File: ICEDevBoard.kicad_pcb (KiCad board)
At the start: 2 copper layers, 9.2 x 1.8 mm, 233 parts, among them J101 USB4215-03-A_REVA, J301 program, J401 VGA, J501 Joystick, J502 SJ2-35813B-SMT-TR, J503 Keyboard, J504 Mouse, J505 MSD-1-A, J701 PMOD, Q101 BC847, SW701 SW_Push, SW702 SW_Push, SW703 SW_Push, U101 AP2127K-3.3, U102 AP2127K-2.5, U103 AP2127K-1.2, U201 93LC56BT-I/OT, U202 FT232H, U301 ICE40HX8K-BG121, U302 W25Q32JVSS, U401 ADV7123, U501 SN74LVC8T245PWR, U502 PCM5102A, U503 SN74LV1T34DBV, U601 IS61WV5128EDBLL-10TLI, U701 74AHC595, U702 74AHC595, Y201 12Mhz, Y301 50Mhz, Y302 12Mhz

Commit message: Started layout
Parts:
- moved H104 414.1 mm to (192.0, 142.0)
- moved H102 391.0 mm to (192.0, 58.0)
- moved C105 345.8 mm to (116.5, 127.5), turned to -90 degrees
- moved H103 344.7 mm to (107.0, 142.0)
- moved C107 339.4 mm to (116.5, 123.5), turned to -90 degrees
- moved D104 338.0 mm to (112.5, 125.5), turned to 180 degrees
- moved R103 336.5 mm to (112.6, 130.5)
- moved L101 335.6 mm to (111.4, 118.0)
- moved R105 330.7 mm to (112.4, 122.0)
- moved TP103 329.2 mm to (115.5, 118.0)
- moved C109 327.0 mm to (106.5, 118.0)
- moved J101 318.3 mm to (102.5, 125.7), turned to -90 degrees
- moved H101 314.5 mm to (107.0, 58.0)
- moved C201 249.7 mm to (115.5, 157.3)
- moved C205 249.7 mm to (115.5, 166.3)
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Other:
- board size 9.2 x 1.8 mm -> 100 x 100 mm

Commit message: Working on board layout
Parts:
- D101, D102, D103, D201, D202, D301, D703, D704, D705: footprint LED_SMD:LED_1210_3225Metric -> LED_SMD:LED_1206_3216Metric
- J401: footprint Connector_Dsub:DSUB-15-HD_Pins_Horizontal_P2.29x2.54mm_EdgePinOffset8.35mm_Housed_MountingHolesOffset10.89mm -> Connector_Dsub:DSUB-15-HD_Socket_Horizontal_P2.29x2.54mm_EdgePinOffset8.35mm_Housed_MountingHolesOffset10.89mm
- moved C512 360.7 mm to (197.4, 136.2)
- moved C513 357.8 mm to (197.4, 123.6), turned to 180 degrees
- moved R101 354.7 mm to (102.5, 110.2)
- moved R102 352.5 mm to (102.4, 106.2)
- moved C509 351.1 mm to (183.1, 134.4)
- moved D105 350.8 mm to (107.0, 98.4)
- moved D101 350.6 mm to (107.0, 110.2)
- moved R104 349.7 mm to (102.4, 102.2)
- moved C508 349.1 mm to (179.3, 134.4)
- moved J502 346.3 mm to (191.4, 129.7), turned to 180 degrees
- moved C507 346.3 mm to (174.1, 135.1)
- moved R107 345.1 mm to (102.5, 98.4)
- moved R106 345.0 mm to (102.7, 94.3)
- moved D102 345.0 mm to (107.0, 106.2)
- moved Q101 344.1 mm to (107.0, 94.0)
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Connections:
- R101 pad 1: Net-(D101-K) -> GND
- R101 pad 2: GND -> Net-(D101-K)

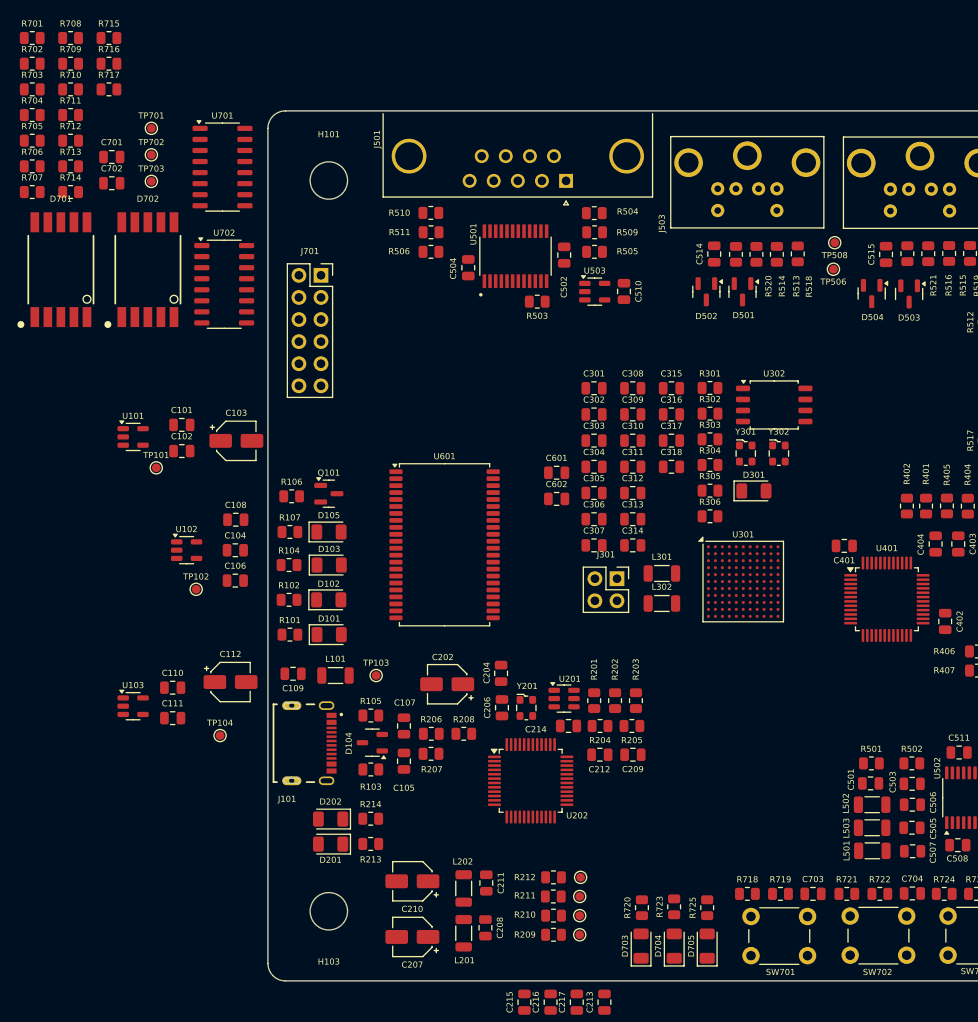
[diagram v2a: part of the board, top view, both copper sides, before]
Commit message: More board layout
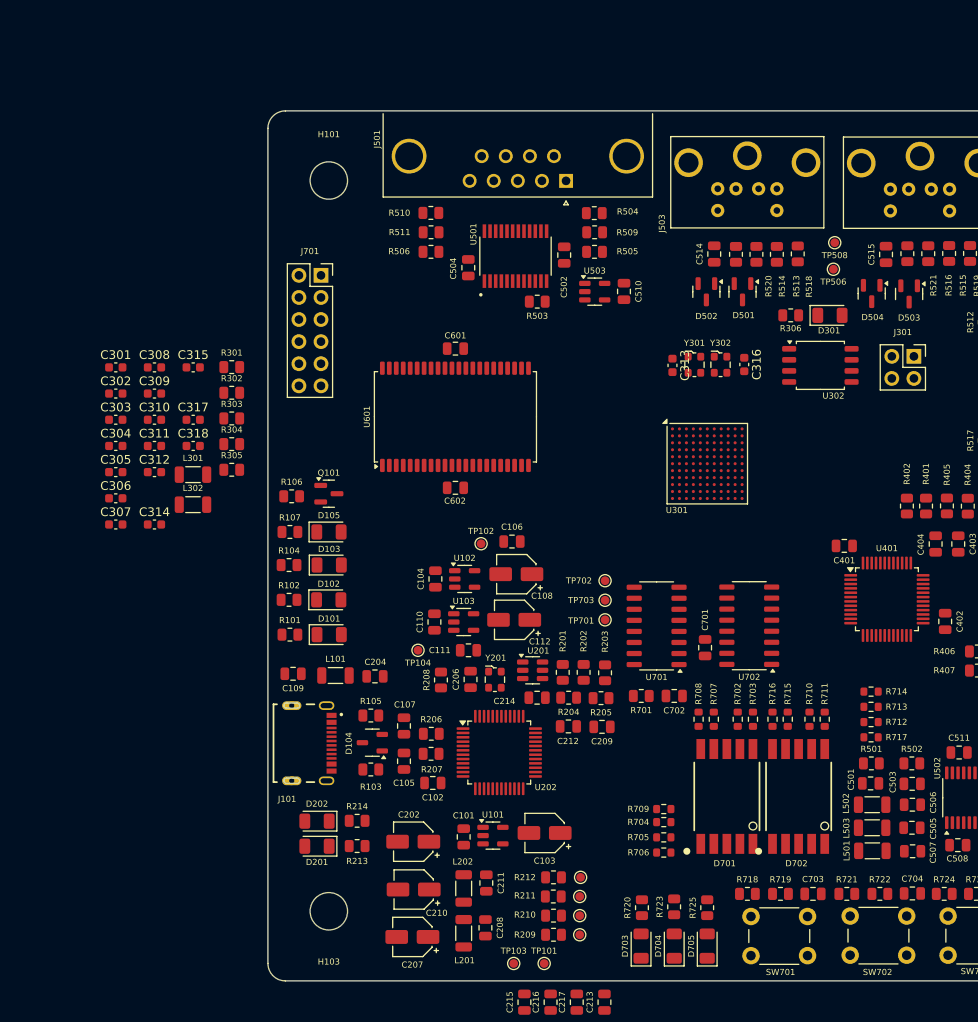
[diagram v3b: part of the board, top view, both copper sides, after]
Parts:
- C108: footprint Capacitor_SMD:C_0805_2012Metric -> Capacitor_SMD:CP_Elec_4x5.3
- C301, C302, C303, C304, C305, C306, C307, C308, C309, C310, C311, C312, C313, C314, C315, C316, C317, C318: footprint Capacitor_SMD:C_0805_2012Metric -> Capacitor_SMD:C_0603_1608Metric
- R206, R207: value 0R -> 22R
- R702, R703, R704, R705, R706, R707, R708, R709, R710, R711, R712, R713, R714, R715, R716, R717: footprint Resistor_SMD:R_0805_2012Metric -> Resistor_SMD:R_0603_1608Metric
- moved R717 115.0 mm to (169.3, 122.0)
- moved R712 113.7 mm to (169.3, 120.2), turned to 180 degrees
- moved R710 111.6 mm to (162.2, 119.9), turned to -90 degrees
- moved R711 111.1 mm to (164.0, 119.9), turned to -90 degrees
- moved R713 111.0 mm to (169.3, 118.5), turned to 180 degrees
- moved R702 110.7 mm to (154.0, 119.9), turned to -90 degrees
- moved R715 110.5 mm to (159.8, 119.9), turned to 90 degrees
- moved R703 110.0 mm to (155.8, 119.9), turned to -90 degrees
- moved R709 109.5 mm to (145.5, 130.2)
- moved R704 109.0 mm to (145.5, 131.8)
- moved R714 108.5 mm to (169.3, 116.8), turned to 180 degrees
- moved R705 108.1 mm to (145.5, 133.5)
- moved R716 107.2 mm to (158.0, 119.9), turned to -90 degrees
- moved R706 107.2 mm to (145.5, 135.2)
- moved R708 106.5 mm to (149.5, 119.9), turned to -90 degrees
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
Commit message: Started FPGA fanout
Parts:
- R702, R703, R704, R705, R706, R707, R708, R709, R710, R711, R712, R713, R714, R715, R716, R717: footprint Resistor_SMD:R_0603_1608Metric -> Resistor_SMD:R_0805_2012Metric
- moved C302 11.2 mm to (83.5, 93.7)
- moved C309 11.2 mm to (88.0, 93.7)
- moved R303 11.2 mm to (96.9, 96.5)
- moved C301 11.2 mm to (83.5, 90.7)
- moved C303 11.2 mm to (83.5, 96.7)
- moved C304 11.2 mm to (83.5, 99.7)
- moved C305 11.2 mm to (83.5, 102.7)
- moved C306 11.2 mm to (83.5, 105.7)
- moved C307 11.2 mm to (83.5, 108.7)
- moved C308 11.2 mm to (88.0, 90.7)
- moved C310 11.2 mm to (88.0, 96.7)
- moved C311 11.2 mm to (88.0, 99.7)
- moved C312 11.2 mm to (88.0, 102.7)
- moved C314 11.2 mm to (88.0, 108.7)
- moved C315 11.2 mm to (92.5, 90.7)
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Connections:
- U301 pad A1: /FPGA/PMOD3 -> unconnected-(U301A-IOT_225-PadA1)
- U301 pad A10: /FPGA/MEM_A1 -> unconnected-(U301A-IOT_170-PadA10)
- U301 pad A11: /FPGA/MEM_A0 -> unconnected-(U301A-IOT_168-PadA11)
- U301 pad A2: /FPGA/PMOD1 -> unconnected-(U301A-IOT_222-PadA2)
- U301 pad A3: /FPGA/PMOD2 -> unconnected-(U301A-IOT_223-PadA3)
- U301 pad A4: /FPGA/MEM_A16 -> unconnected-(U301A-IOT_211-PadA4)
- U301 pad A5: /FPGA/MEM_A14 -> unconnected-(U301A-IOT_207-PadA5)
- U301 pad A6: /FPGA/MEM_A13 -> unconnected-(U301A-IOT_206-PadA6)
- U301 pad A7: /FPGA/MEM_A10 -> unconnected-(U301A-IOT_192-PadA7)
- U301 pad A8: /FPGA/MEM_A8 -> unconnected-(U301A-IOT_190-PadA8)
- U301 pad A9: /FPGA/MEM_A5 -> unconnected-(U301A-IOT_178-PadA9)
- U301 pad B1: /FPGA/VGA_R0 -> unconnected-(U301D-IOL_2A-PadB1)
- U301 pad B11: /FPGA/PMOD4 -> unconnected-(U301B-IOR_161-PadB11)
- U301 pad B2: /FPGA/VGA_R1 -> unconnected-(U301D-IOL_2B-PadB2)
- U301 pad B3: /FPGA/PMOD0 -> unconnected-(U301A-IOT_221-PadB3)
- U301 pad B4: /FPGA/MEM_A18 -> unconnected-(U301A-IOT_219-PadB4)
- U301 pad B5: /FPGA/MEM_A15 -> unconnected-(U301A-IOT_208-PadB5)
- U301 pad B8: /FPGA/MEM_A4 -> unconnected-(U301A-IOT_177-PadB8)
- U301 pad B9: /FPGA/MEM_A3 -> unconnected-(U301A-IOT_174-PadB9)
- U301 pad C1: /FPGA/VGA_G0 -> unconnected-(U301D-IOL_5B-PadC1)
- U301 pad C11: /FPGA/JOY_D5 -> unconnected-(U301B-IOR_160-PadC11)
- U301 pad C2: /FPGA/VGA_R4 -> unconnected-(U301D-IOL_5A-PadC2)
- U301 pad C3: /FPGA/VGA_R3 -> unconnected-(U301D-IOL_4B-PadC3)
- U301 pad C4: /FPGA/VGA_R2 -> unconnected-(U301D-IOL_4A-PadC4)
- U301 pad C7: /FPGA/MEM_A9 -> unconnected-(U301A-IOT_191-PadC7)
- U301 pad C8: /FPGA/MEM_A6 -> unconnected-(U301A-IOT_179-PadC8)
- U301 pad C9: /FPGA/MEM_A2 -> unconnected-(U301A-IOT_172-PadC9)
- U301 pad D1: /FPGA/VGA_G2 -> unconnected-(U301D-IOL_8B-PadD1)
- U301 pad D10: /FPGA/JOY_D4 -> unconnected-(U301B-IOR_154-PadD10)
- U301 pad D11: /FPGA/JOY_D3 -> unconnected-(U301B-IOR_152-PadD11)
- U301 pad D2: /FPGA/VGA_G3 -> unconnected-(U301D-IOL_9A-PadD2)
- U301 pad D3: /FPGA/VGA_G4 -> unconnected-(U301D-IOL_9B-PadD3)
- U301 pad D5: /FPGA/MEM_A17 -> unconnected-(U301A-IOT_212-PadD5)
- U301 pad D7: /FPGA/MEM_A7 -> unconnected-(U301A-IOT_181-PadD7)
- U301 pad D9: /FPGA/JOY_D1 -> unconnected-(U301B-IOR_147-PadD9)
- U301 pad E1: /FPGA/VGA_G1 -> unconnected-(U301D-IOL_8A-PadE1)
- U301 pad E10: /FPGA/SND_BCK -> unconnected-(U301B-IOR_141_GBIN2-PadE10)
- U301 pad E11: /FPGA/JOY_D2 -> unconnected-(U301B-IOR_148-PadE11)
- U301 pad E2: /FPGA/VGA_G5 -> unconnected-(U301D-IOL_10A-PadE2)
- U301 pad E3: /FPGA/VGA_B0 -> unconnected-(U301D-IOL_10B-PadE3)
- U301 pad E8: /FPGA/JOY_D0 -> unconnected-(U301B-IOR_146-PadE8)
- U301 pad E9: /FPGA/JOY_SEL -> unconnected-(U301B-IOR_144-PadE9)
- U301 pad F1: /FPGA/VGA_B1 -> unconnected-(U301D-IOL_12A-PadF1)
- U301 pad F10: /FPGA/~{SRAM_WE} -> unconnected-(U301B-IOR_136-PadF10)
- U301 pad F11: /FPGA/SND_DIN -> unconnected-(U301B-IOR_140_GBIN3-PadF11)
- U301 pad F2: /FPGA/VGA_B2 -> unconnected-(U301D-IOL_12B-PadF2)
- U301 pad F3: /FPGA/VGA_B4 -> unconnected-(U301D-IOL_13B_GBIN7-PadF3)
- U301 pad F4: /FPGA/VGA_B3 -> unconnected-(U301D-IOL_13A-PadF4)
- U301 pad F9: /FPGA/SND_LRCK -> unconnected-(U301B-IOR_137-PadF9)
- U301 pad G1: /FPGA/~{VGA_BLANK} -> unconnected-(U301D-IOL_14A_GBIN6-PadG1)
- U301 pad G10: /FPGA/MEM_D6 -> unconnected-(U301B-IOR_120-PadG10)
- U301 pad G11: /FPGA/~{SRAM_CE} -> unconnected-(U301B-IOR_129-PadG11)
- U301 pad G2: /FPGA/VGA_CLOCK -> unconnected-(U301D-IOL_14B-PadG2)
- U301 pad G3: /FPGA/VGA_HSYNC -> unconnected-(U301D-IOL_17A-PadG3)
- U301 pad G8: /FPGA/MEM_D4 -> unconnected-(U301B-IOR_118-PadG8)
- U301 pad G9: /FPGA/MEM_D7 -> unconnected-(U301B-IOR_128-PadG9)
- U301 pad H1: /FPGA/BUTTON1 -> unconnected-(U301D-IOL_18A-PadH1)
- U301 pad H10: /FPGA/MEM_D2 -> unconnected-(U301B-IOR_116-PadH10)
- U301 pad H11: /FPGA/MEM_D5 -> unconnected-(U301B-IOR_119-PadH11)
- U301 pad H2: /FPGA/BUTTON2 -> unconnected-(U301D-IOL_18B-PadH2)
- U301 pad H3: /FPGA/VGA_VSYNC -> unconnected-(U301D-IOL_17B-PadH3)
- U301 pad H7: /FPGA/LED2 -> unconnected-(U301C-IOB_87-PadH7)
- U301 pad H9: /FPGA/PMOD7 -> unconnected-(U301C-IOB_104_CBSEL1-PadH9)
- U301 pad J1: /FPGA/BUTTON3 -> unconnected-(U301D-IOL_23A-PadJ1)
- U301 pad J10: /FPGA/MEM_D3 -> unconnected-(U301B-IOR_117-PadJ10)
- U301 pad J11: /FPGA/MEM_D0 -> unconnected-(U301B-IOR_114-PadJ11)
- U301 pad J2: /FPGA/MEM_A12 -> unconnected-(U301D-IOL_25B-PadJ2)
- U301 pad J3: /FPGA/KBD_DATA -> unconnected-(U301C-IOB_57-PadJ3)
- U301 pad J4: /FPGA/SEG_DATA -> unconnected-(U301C-IOB_64-PadJ4)
- U301 pad J5: /FPGA/SD_MOSI -> unconnected-(U301C-IOB_78-PadJ5)
- U301 pad J7: /FPGA/LED1 -> unconnected-(U301C-IOB_86-PadJ7)
- U301 pad K11: /FPGA/MEM_D1 -> unconnected-(U301B-IOR_115-PadK11)
- U301 pad K2: /FPGA/MEM_A11 -> unconnected-(U301D-IOL_25A-PadK2)
- U301 pad K3: /FPGA/MOUSE_DATA -> unconnected-(U301C-IOB_63-PadK3)
- U301 pad K4: /FPGA/SD_SELECT -> unconnected-(U301C-IOB_73-PadK4)
- U301 pad K5: /FPGA/SD_CLOCK -> unconnected-(U301C-IOB_79-PadK5)
- U301 pad K6: /FPGA/SD_DETECT -> unconnected-(U301C-IOB_82_GBIN4-PadK6)
- U301 pad K7: /FPGA/LED3 -> unconnected-(U301C-IOB_89-PadK7)
- U301 pad L1: /FPGA/KBD_CLK -> unconnected-(U301C-IOB_56-PadL1)
- U301 pad L2: /FPGA/MOUSE_CLK -> unconnected-(U301C-IOB_61-PadL2)
- U301 pad L3: /FPGA/SEG_CLK -> unconnected-(U301C-IOB_71-PadL3)
- U301 pad L4: /FPGA/SEG_LOAD -> unconnected-(U301C-IOB_72-PadL4)
- U301 pad L5: /FPGA/SD_MISO -> unconnected-(U301C-IOB_81_GBIN5-PadL5)
- U301 pad L7: /FPGA/PMOD5 -> unconnected-(U301C-IOB_94-PadL7)
- U301 pad L8: /FPGA/PMOD6 -> unconnected-(U301C-IOB_103_CBSEL0-PadL8)
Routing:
- net unconnected-(U301C-IOB_81_GBIN5-PadL5): track 0.00 -> 1.60 mm
- net unconnected-(U301C-IOB_72-PadL4): track 0.00 -> 1.60 mm
- net unconnected-(U301C-IOB_71-PadL3): track 0.00 -> 1.60 mm
- net unconnected-(U301D-IOL_8B-PadD1): track 0.00 -> 1.55 mm
- net unconnected-(U301D-IOL_8A-PadE1): track 0.00 -> 1.55 mm
- net unconnected-(U301D-IOL_5B-PadC1): track 0.00 -> 1.55 mm
- net unconnected-(U301D-IOL_2A-PadB1): track 0.00 -> 1.55 mm
- net unconnected-(U301D-IOL_23B-PadK1): track 0.00 -> 1.55 mm
- net unconnected-(U301D-IOL_23A-PadJ1): track 0.00 -> 1.55 mm
- net unconnected-(U301D-IOL_18A-PadH1): track 0.00 -> 1.55 mm
- net unconnected-(U301D-IOL_14A_GBIN6-PadG1): track 0.00 -> 1.55 mm
- net unconnected-(U301D-IOL_12A-PadF1): track 0.00 -> 1.55 mm
- net unconnected-(U301B-IOR_161-PadB11): track 0.00 -> 1.55 mm
- net unconnected-(U301B-IOR_160-PadC11): track 0.00 -> 1.55 mm
- net unconnected-(U301B-IOR_148-PadE11): track 0.00 -> 1.55 mm
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- added copper zone on In1.Cu, net GND
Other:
- copper layers 2 -> 4

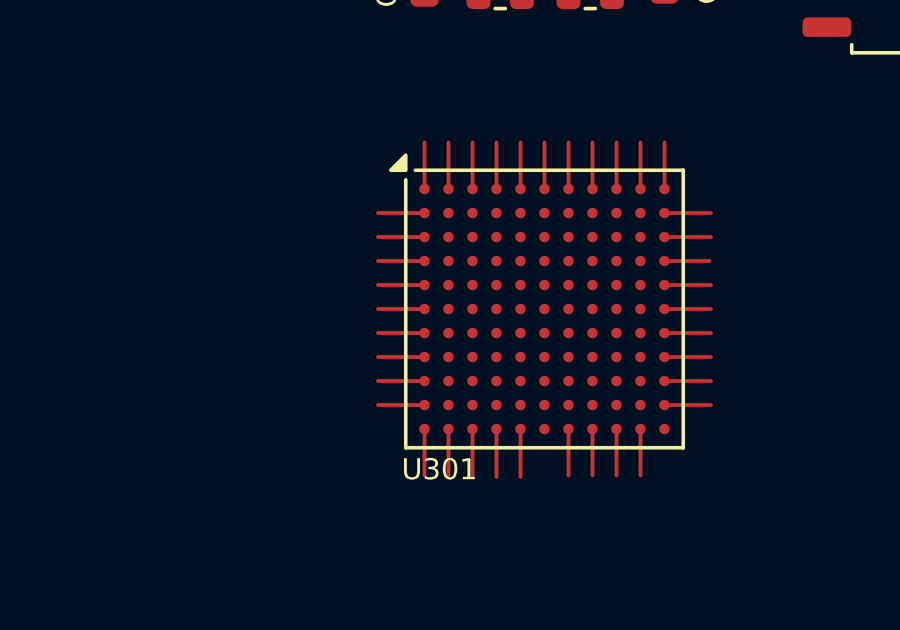
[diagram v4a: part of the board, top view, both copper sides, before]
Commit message: Updated constraints
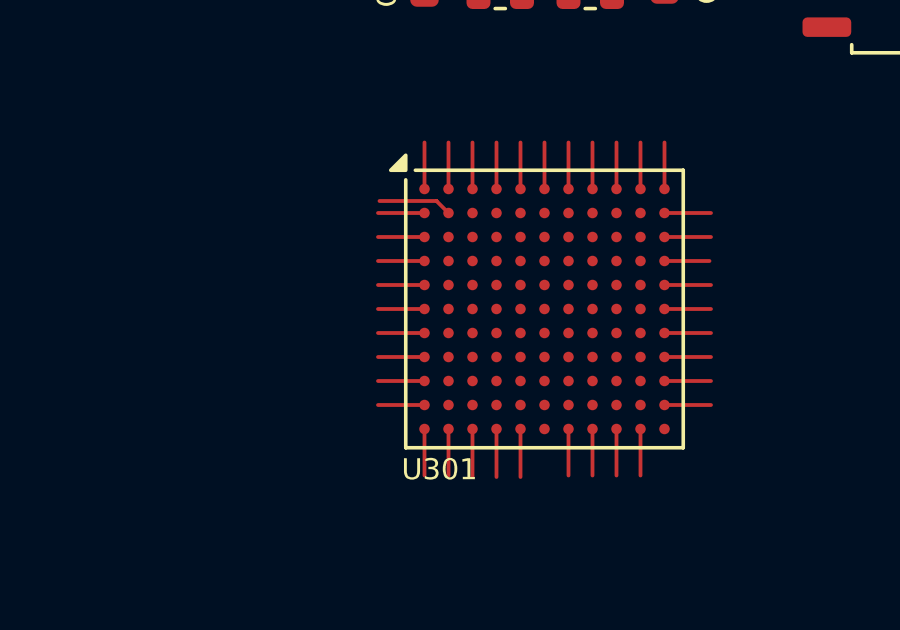
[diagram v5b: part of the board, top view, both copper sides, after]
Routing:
- net unconnected-(U301D-IOL_2B-PadB2): track 0.00 -> 2.47 mm
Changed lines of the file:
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@@
+	)
+	(segment
+		(start 147.3 87.35)
+		(end 146.9 86.95)
+		(width 0.127)
+		(layer "F.Cu")
+		(net 282)
+	)
+	(segment
+		(start 146.9 86.95)
+		(end 145 86.95)
+		(width 0.127)
+		(layer "F.Cu")
+		(net 282)
 	)
 	(segment
@@
 		(width 0.127)
 		(layer "F.Cu")
+		(net 287)
+	)
+	(segment
+		(start 149.7 94.55)
+		(end 149.7 94.527822)
+		(width 0.127)
+		(layer "F.Cu")

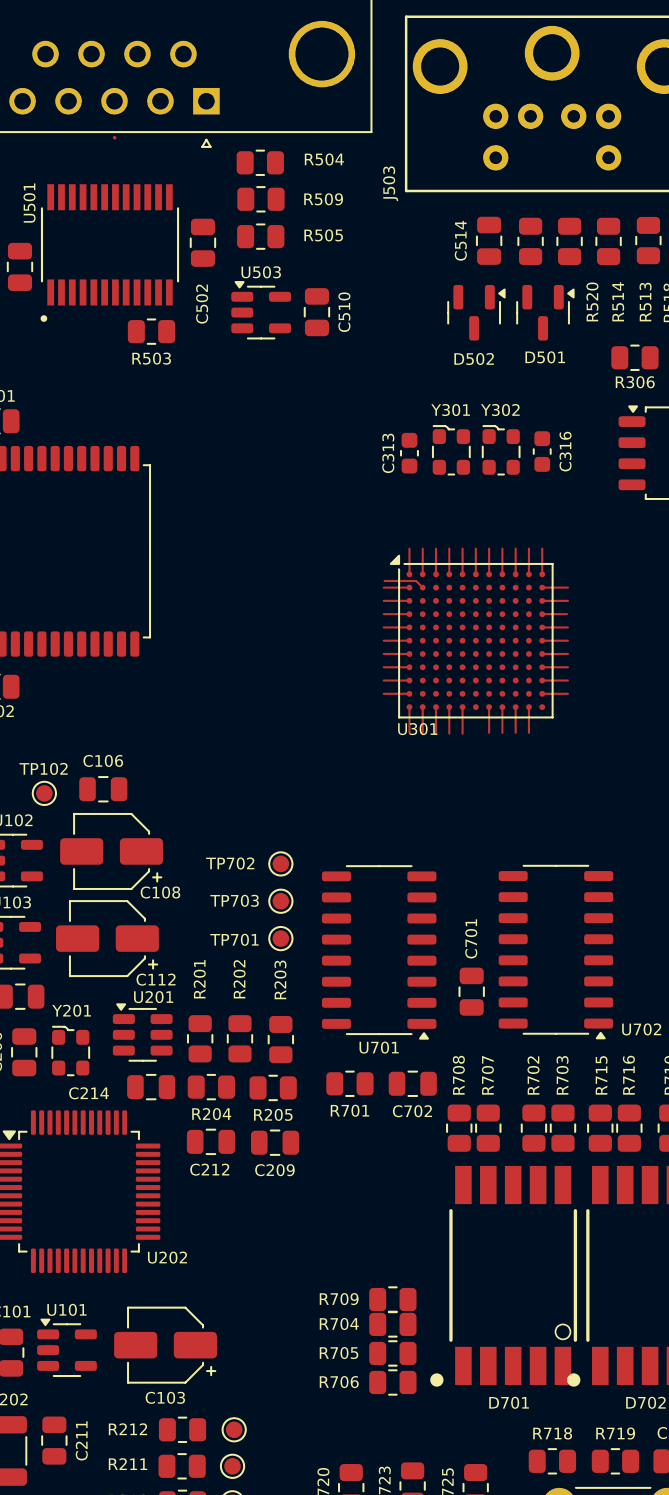
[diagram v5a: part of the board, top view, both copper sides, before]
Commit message: All pins fed out of FPGA
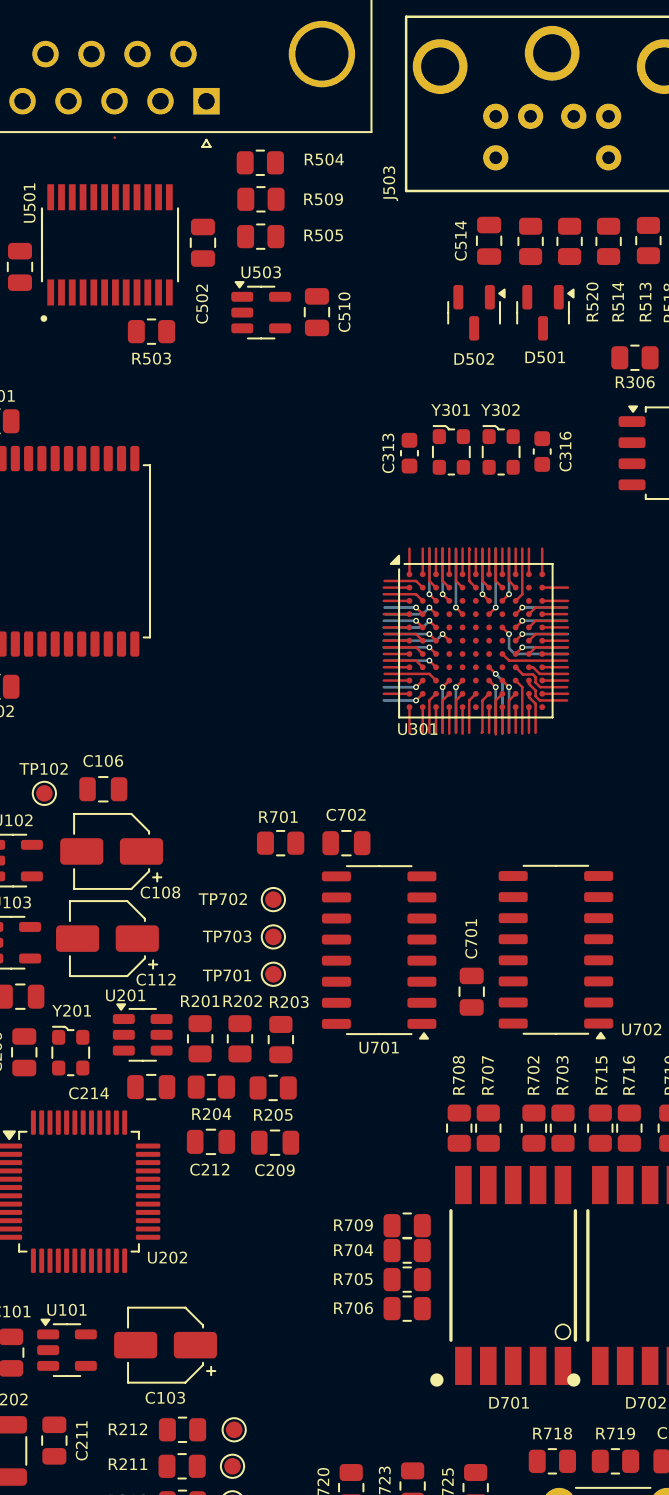
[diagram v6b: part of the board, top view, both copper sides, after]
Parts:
- moved R701 15.1 mm to (138.7, 102.8)
- moved C702 15.0 mm to (142.7, 102.8), turned to 0 degrees
- moved R704 4.53 mm to (146.4, 127.3)
- moved R709 4.53 mm to (146.4, 125.8)
- moved R705 4.53 mm to (146.4, 129.1)
- moved R706 4.53 mm to (146.4, 130.8)
- moved TP701 2.20 mm to (138.3, 110.7)
- moved TP702 2.20 mm to (138.3, 106.2)
- moved TP703 2.20 mm to (138.3, 108.4)
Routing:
- net unconnected-(U301B-IOR_146-PadE8): track 0.00 -> 5.11 mm, vias 0 -> 1
- net unconnected-(U301C-IOB_87-PadH7): track 0.00 -> 4.33 mm, vias 0 -> 1
- net unconnected-(U301D-IOL_13A-PadF4): track 0.00 -> 4.28 mm, vias 0 -> 1
- net unconnected-(U301A-IOT_181-PadD7): track 0.00 -> 4.12 mm, vias 0 -> 1
- net unconnected-(U301B-IOR_118-PadG8): track 0.00 -> 4.07 mm
- net unconnected-(U301A-IOT_212-PadD5): track 0.00 -> 4.07 mm, vias 0 -> 1
- net unconnected-(U301C-IOB_104_CBSEL1-PadH9): track 0.00 -> 3.78 mm
- net unconnected-(U301D-IOL_9B-PadD3): track 0.00 -> 3.53 mm, vias 0 -> 1
- net unconnected-(U301D-IOL_10B-PadE3): track 0.00 -> 3.48 mm, vias 0 -> 1
- net unconnected-(U301C-IOB_78-PadJ5): track 0.00 -> 3.39 mm, vias 0 -> 1
- net /FPGA/FPGA_SI: track 0.00 -> 3.37 mm
- net unconnected-(U301D-IOL_4B-PadC3): track 0.00 -> 3.32 mm, vias 0 -> 1
- net unconnected-(U301D-IOL_4A-PadC4): track 0.00 -> 3.32 mm, vias 0 -> 1
- net unconnected-(U301A-IOT_179-PadC8): track 0.00 -> 3.32 mm, vias 0 -> 1
- net unconnected-(U301A-IOT_172-PadC9): track 0.00 -> 3.32 mm
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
